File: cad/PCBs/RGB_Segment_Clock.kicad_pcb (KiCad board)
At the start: 2 copper layers, 7 parts, among them J1 TYPE-C-31-M-12, U1 BH1750FVI-TR, U2 HDC2080

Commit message: Initial Digit Schematic and Layout
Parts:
- added C1: 0.1 uF, Capacitor_SMD:C_0805_2012Metric, F.Cu at (176.9, 55.0)
- added C10: 0.1 uF, Capacitor_SMD:C_0805_2012Metric, F.Cu at (204.0, 25.4)
- added C11: 0.1 uF, Capacitor_SMD:C_0805_2012Metric, F.Cu at (218.9, 29.5)
- added C12: 0.1 uF, Capacitor_SMD:C_0805_2012Metric, F.Cu at (175.4, 133.0)
- added C13: 0.1 uF, Capacitor_SMD:C_0805_2012Metric, F.Cu at (198.5, 133.5)
- added C14: 0.1 uF, Capacitor_SMD:C_0805_2012Metric, F.Cu at (218.9, 132.5)
- added C2: 0.1 uF, Capacitor_SMD:C_0805_2012Metric, F.Cu at (197.0, 39.0)
- added C3: 0.1 uF, Capacitor_SMD:C_0805_2012Metric, F.Cu at (219.4, 55.0)
- added C4: 0.1 uF, Capacitor_SMD:C_0805_2012Metric, F.Cu at (220.4, 84.0)
- added C5: 0.1 uF, Capacitor_SMD:C_0805_2012Metric, F.Cu at (197.4, 103.0)
- added C6: 0.1 uF, Capacitor_SMD:C_0805_2012Metric, F.Cu at (177.9, 82.0)
- added C7: 0.1 uF, Capacitor_SMD:C_0805_2012Metric, F.Cu at (199.9, 69.5)
- added C8: 0.1 uF, Capacitor_SMD:C_0805_2012Metric, F.Cu at (177.1, 104.5)
- added C9: 0.1 uF, Capacitor_SMD:C_0805_2012Metric, F.Cu at (177.9, 29.5)
- added D2: SS310, Diode_SMD:D_SOD-323F, F.Cu at (166.1, 74.5)
- added D3: SS310, Diode_SMD:D_SOD-323F, F.Cu at (231.4, 70.5)
- added J2: Digit_OUT, Connector_PinHeader_2.54mm:PinHeader_1x06_P2.54mm_Horizontal, F.Cu at (239.1, 55.1)
- added LED1: DIGIT-A, LED_SMD:LED_SK6812_PLCC4_5.0x5.0mm_P3.2mm, B.Cu at (218.6, 47.1)
- added LED10: BL-2, LED_SMD:LED_SK6812_PLCC4_5.0x5.0mm_P3.2mm, F.Cu at (198.5, 22.1)
- added LED11: BL-3, LED_SMD:LED_SK6812_PLCC4_5.0x5.0mm_P3.2mm, F.Cu at (220.0, 22.1)
- added LED12: BL-4, LED_SMD:LED_SK6812_PLCC4_5.0x5.0mm_P3.2mm, F.Cu at (177.0, 124.6)
- added LED13: BL-5, LED_SMD:LED_SK6812_PLCC4_5.0x5.0mm_P3.2mm, F.Cu at (199.5, 124.9)
- added LED14: BL-6, LED_SMD:LED_SK6812_PLCC4_5.0x5.0mm_P3.2mm, F.Cu at (220.0, 124.9)
- added LED2: DIGIT-B, LED_SMD:LED_SK6812_PLCC4_5.0x5.0mm_P3.2mm, B.Cu at (198.6, 31.6)
- added LED3: DIGIT-C, LED_SMD:LED_SK6812_PLCC4_5.0x5.0mm_P3.2mm, B.Cu at (177.0, 46.9)
- added LED4: DIGIT-D, LED_SMD:LED_SK6812_PLCC4_5.0x5.0mm_P3.2mm, B.Cu at (175.5, 76.1)
- added LED5: DIGIT-E, LED_SMD:LED_SK6812_PLCC4_5.0x5.0mm_P3.2mm, B.Cu at (198.0, 95.4)
- added LED6: DIGIT-F, LED_SMD:LED_SK6812_PLCC4_5.0x5.0mm_P3.2mm, B.Cu at (217.6, 73.9)
- added LED7: DIGIT-G, LED_SMD:LED_SK6812_PLCC4_5.0x5.0mm_P3.2mm, B.Cu at (195.5, 61.4)
- added LED8: DIGIT-H, LED_SMD:LED_SK6812_PLCC4_5.0x5.0mm_P3.2mm, B.Cu at (218.0, 96.6)
- added LED9: BL-1, LED_SMD:LED_SK6812_PLCC4_5.0x5.0mm_P3.2mm, F.Cu at (179.0, 21.6)
- added SZ720788W1: ~, SZ720788W:SZ720788W, B.Cu at (115.5, 39.1)
- added U3: BH1750FVI-TR, BH1750FVI-TR:XDCR_BH1750FVI-TR, B.Cu at (108.0, 21.5)
- added U4: HDC2080, Package_SON:Texas_PWSON-N6, B.Cu at (123.2, 20.9)
- added USB1: TYPE-C-31-M-12, TYPE-C-31-M-12:HRO_TYPE-C-31-M-12, F.Cu at (115.0, 135.0)
- D1: moved to B.Cu
- J1: value TYPE-C-31-M-12 -> Digit_IN; footprint TYPE-C-31-M-12:HRO_TYPE-C-31-M-12 -> Connector_PinHeader_2.54mm:PinHeader_1x06_P2.54mm_Horizontal
- U1: value BH1750FVI-TR -> 74HC595; footprint BH1750FVI-TR:XDCR_BH1750FVI-TR -> Package_DIP:DIP-16_W7.62mm_Socket
- U2: value HDC2080 -> 74HC595; footprint Package_SON:Texas_PWSON-N6 -> Package_DIP:DIP-16_W7.62mm_Socket
- moved R2 121.2 mm to (125.5, 128.2), turned to -90 degrees
- moved R1 114.0 mm to (105.5, 128.3), turned to 90 degrees
- moved J1 111.8 mm to (161.0, 55.0)
- moved D1 102.0 mm to (101.5, 122.0), turned to 180 degrees
- moved U2 97.7 mm to (131.8, 93.9), turned to 180 degrees
- moved U1 88.1 mm to (131.6, 70.7), turned to 180 degrees
- moved A1 79.4 mm to (110.5, 91.0)
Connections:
- R1 pad 2: Net-(J1-CC1) -> Net-(USB1-CC1)
- R2 pad 1: Net-(J1-CC2) -> Net-(USB1-CC2)
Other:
- board outline added: 145.5 x 124 mm

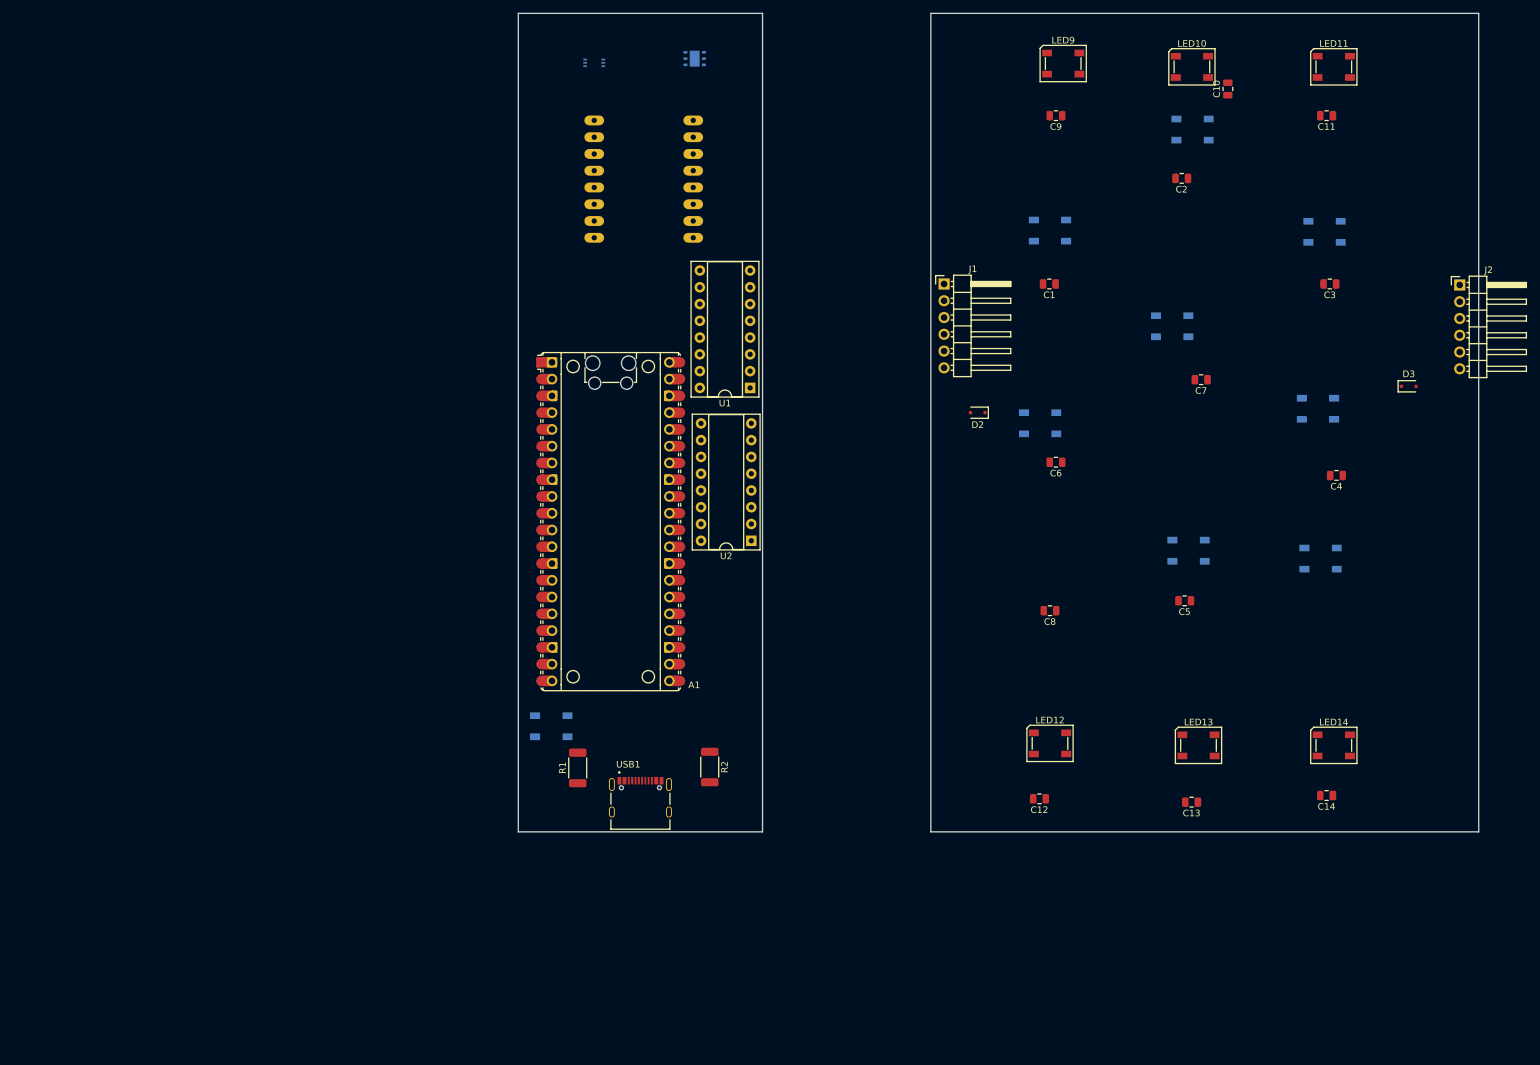
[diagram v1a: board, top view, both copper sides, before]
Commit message: Initial Digit Component Placement
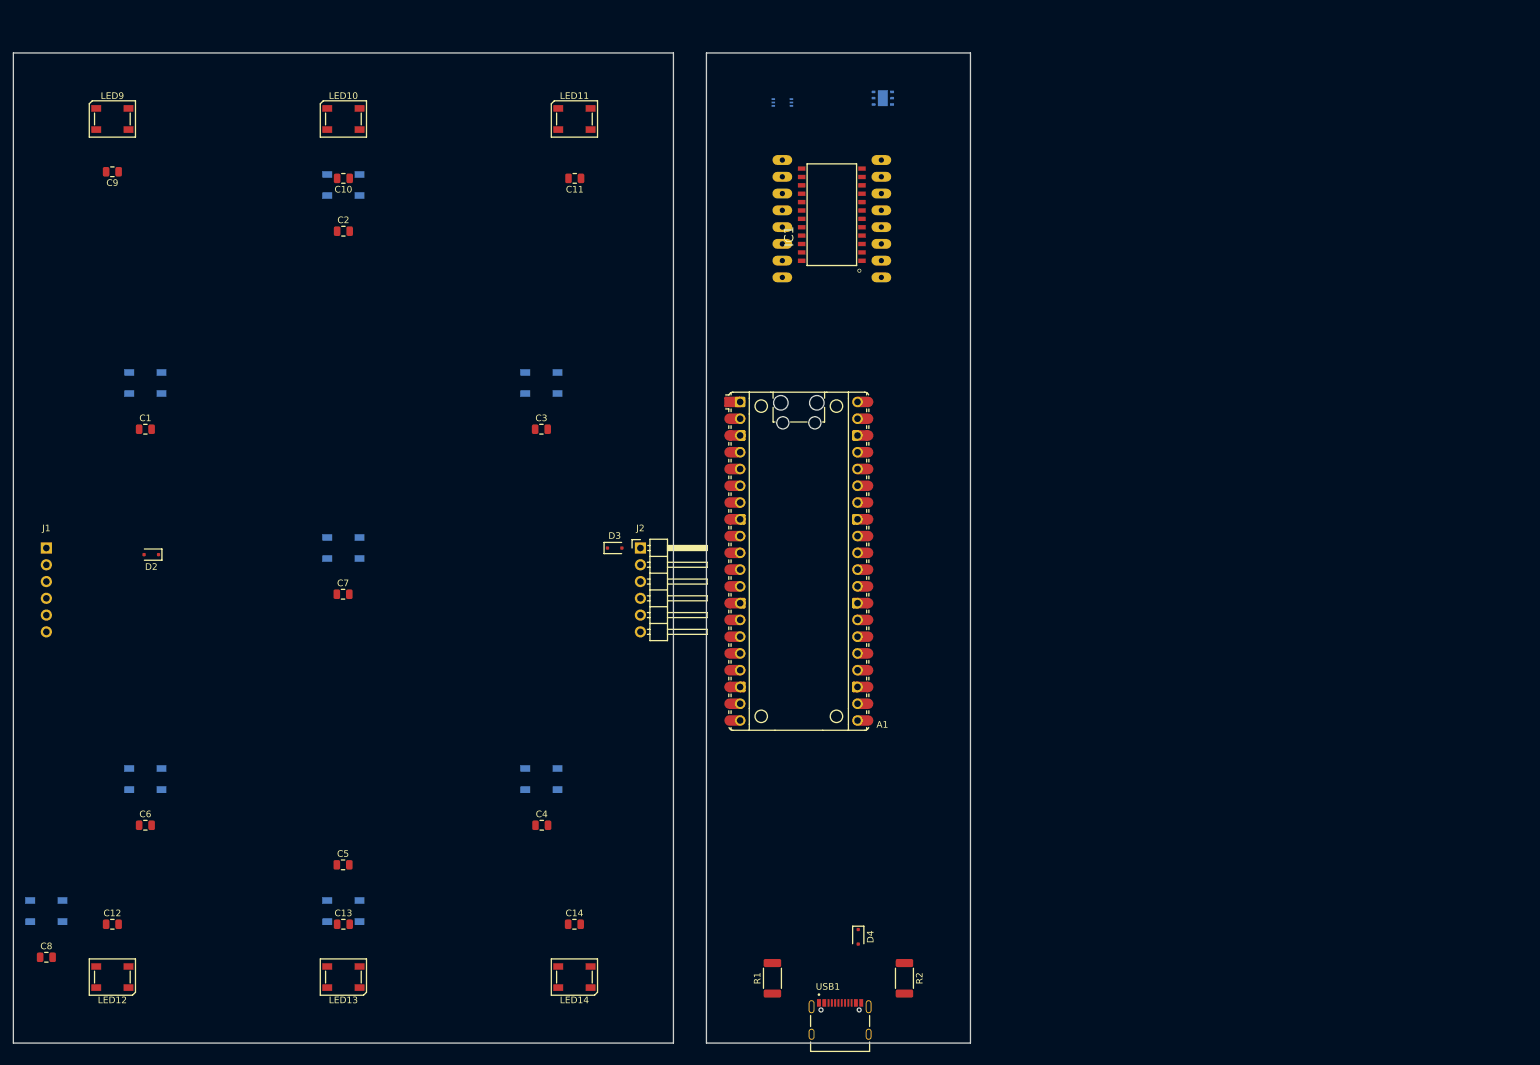
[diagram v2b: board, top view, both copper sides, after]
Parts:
- removed D1: SK6812, LED_SMD:LED_SK6812_PLCC4_5.0x5.0mm_P3.2mm
- removed U1, U2: 74HC595, Package_DIP:DIP-16_W7.62mm_Socket
- added D4: SS310, Diode_SMD:D_SOD-323F, F.Cu at (148.0, 153.9)
- added IC1: HT16K33, HT16K33:HT16K33, F.Cu at (144.0, 44.5)
- J1: moved to B.Cu
- moved LED8 200.3 mm to (25.0, 150.0)
- moved LED6 186.3 mm to (40.0, 130.0)
- moved LED1 180.1 mm to (40.0, 70.0)
- moved C8 160.9 mm to (25.0, 157.0), turned to 0 degrees
- moved C6 148.5 mm to (40.0, 137.0), turned to 0 degrees
- moved LED12 146.4 mm to (35.0, 160.0), turned to 180 degrees
- moved LED9 144.3 mm to (35.0, 30.0)
- moved C9 143.2 mm to (35.0, 38.0)
- moved J1 141.8 mm to (25.0, 95.0), turned to 180 degrees
- moved C12 141.7 mm to (35.0, 152.0), turned to 0 degrees
- moved LED5 139.2 mm to (70.0, 150.0)
- moved C1 138.7 mm to (40.0, 77.0), turned to 0 degrees
- moved C10 134.7 mm to (70.0, 39.0), turned to 180 degrees
- moved LED13 134.2 mm to (70.0, 160.0), turned to 180 degrees
- moved C7 134.0 mm to (70.0, 102.0), turned to 0 degrees
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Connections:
- A1 pad 39: unconnected-(A1-VSYS-Pad39) -> +5V
- USB1 pad A4_B9: +5V -> Net-(D4-A)
- USB1 pad B4_A9: +5V -> Net-(D4-A)
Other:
- board size 145.5 x 124 mm -> 145 x 150 mm

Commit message: Connected Controller Components, updated matrix footprint
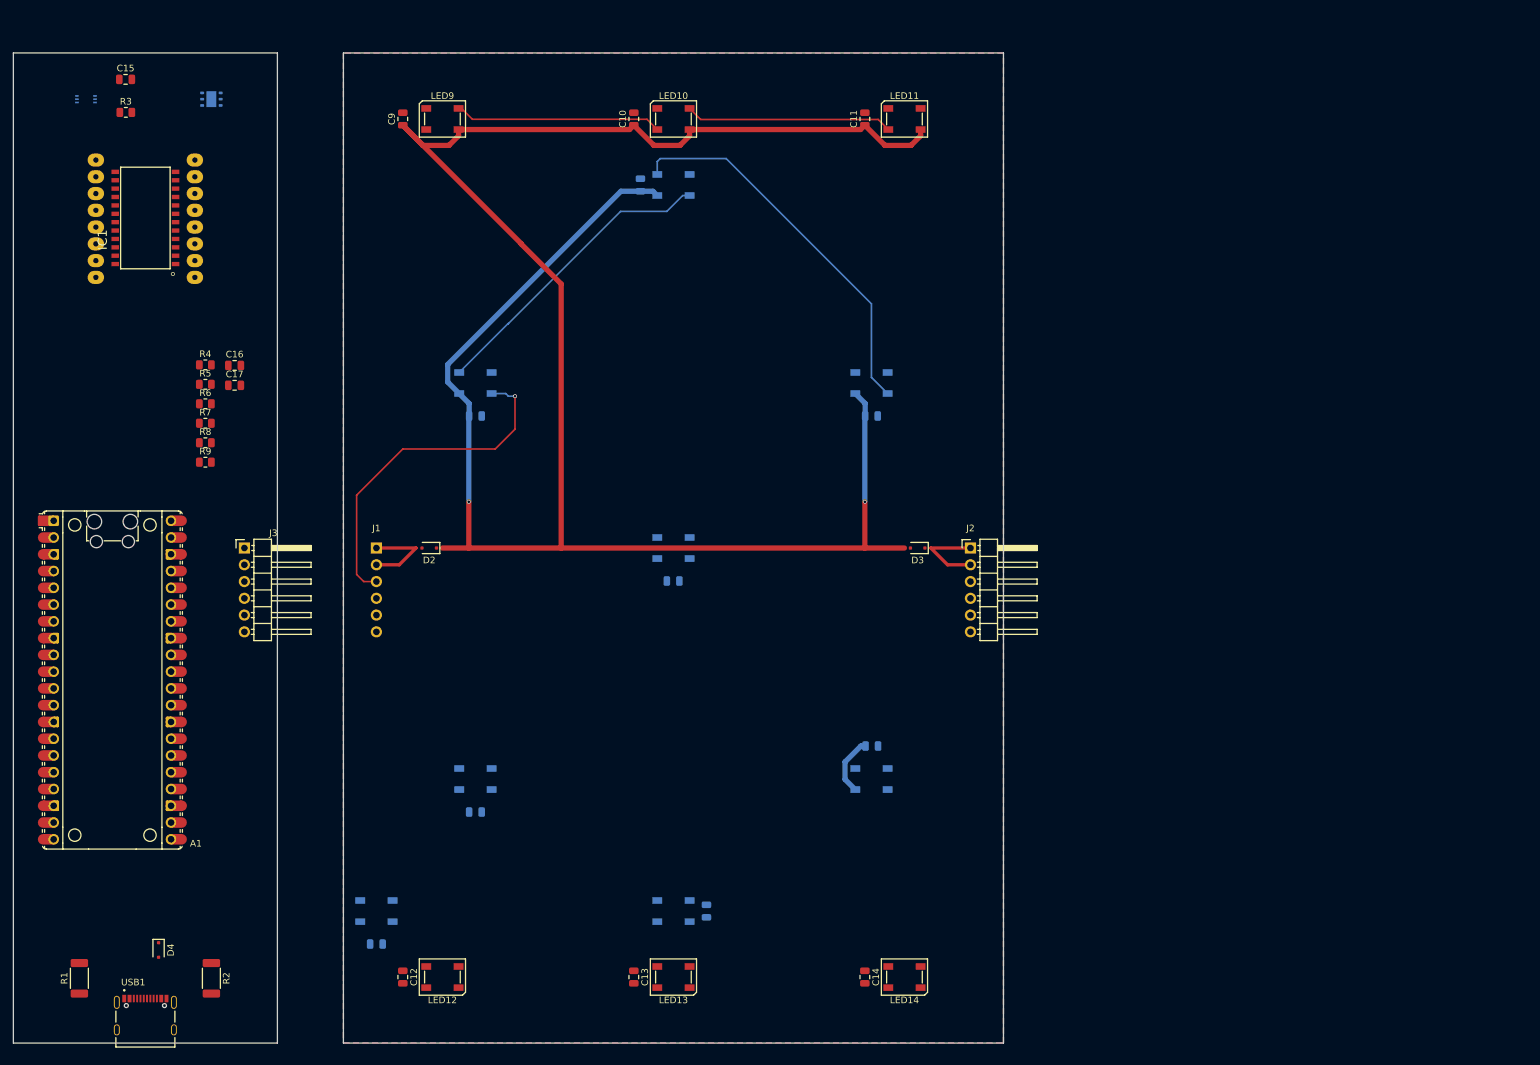
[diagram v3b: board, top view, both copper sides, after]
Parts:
- added C15: 0.1 uF, Capacitor_SMD:C_0805_2012Metric, F.Cu at (37.0, 24.0)
- added C16: 0.1 uF, Capacitor_SMD:C_0805_2012Metric, F.Cu at (53.5, 67.3)
- added C17: 10uF, Capacitor_SMD:C_0805_2012Metric, F.Cu at (53.5, 70.3)
- added J3: Controller_Out, Connector_PinHeader_2.54mm:PinHeader_1x06_P2.54mm_Horizontal, F.Cu at (55.0, 95.0)
- added R3: 4.7k, Resistor_SMD:R_0805_2012Metric, F.Cu at (37.0, 29.0)
- added R4: 4.7k, Resistor_SMD:R_0805_2012Metric, F.Cu at (49.1, 67.2)
- added R5: 4.7k, Resistor_SMD:R_0805_2012Metric, F.Cu at (49.1, 70.2)
- added R6: 4.7k, Resistor_SMD:R_0805_2012Metric, F.Cu at (49.1, 73.2)
- added R7: 4.7k, Resistor_SMD:R_0805_2012Metric, F.Cu at (49.1, 76.1)
- added R8: 4.7k, Resistor_SMD:R_0805_2012Metric, F.Cu at (49.1, 79.0)
- added R9: 4.7k, Resistor_SMD:R_0805_2012Metric, F.Cu at (49.1, 82.0)
- C1, C2, C3, C4, C5, C6, C7, C8: moved to B.Cu
- moved D4 106.0 mm to (42.0, 155.9)
- moved A1 105.5 mm to (35.0, 115.0)
- moved U3 105.5 mm to (31.0, 27.0)
- moved USB1 105.3 mm to (40.0, 168.0)
- moved R1 105.0 mm to (30.0, 160.2)
- moved R2 105.0 mm to (50.0, 160.2)
- moved IC1 104.0 mm to (40.0, 45.0)
- moved SZ720788W1 104.0 mm to (40.0, 45.0)
- moved U4 101.7 mm to (50.0, 27.0)
- moved C5 55.5 mm to (125.0, 150.0), turned to 90 degrees
- moved C4 51.4 mm to (150.1, 125.0)
- moved C1 50.0 mm to (90.0, 75.0)
- moved C3 50.0 mm to (150.0, 75.0)
- moved C6 50.0 mm to (90.0, 135.0)
- moved C7 50.0 mm to (120.0, 100.0)
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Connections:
- A1 pad 21: unconnected-(A1-GPIO16-Pad21) -> /Controller/DIGIT_OUT
- A1 pad 22: unconnected-(A1-GPIO17-Pad22) -> /Controller/BL_OUT
- A1 pad 24: unconnected-(A1-GPIO18-Pad24) -> /Controller/MATRIX_SDA
- A1 pad 25: unconnected-(A1-GPIO19-Pad25) -> /Controller/MATRIX_SCL
- A1 pad 26: unconnected-(A1-GPIO20-Pad26) -> /Controller/SENSOR_SDA
- A1 pad 27: unconnected-(A1-GPIO21-Pad27) -> /Controller/SENSOR_SCL
- A1 pad 33: unconnected-(A1-AGND-Pad33) -> GND
- A1 pad 36: unconnected-(A1-3V3-Pad36) -> +3.3V
- D2 pad 2: /Digit/VCC_IN -> +5V
- IC1 pad 1: unconnected-(IC1-VSS-Pad1) -> GND
- IC1 pad 14: unconnected-(IC1-ROW7/K6-Pad14) -> Net-(IC1-ROW7/K6)
- IC1 pad 15: unconnected-(IC1-ROW6/K5-Pad15) -> Net-(IC1-ROW6/K5)
- IC1 pad 16: unconnected-(IC1-ROW5/K4-Pad16) -> Net-(IC1-ROW5/K4)
- IC1 pad 17: unconnected-(IC1-ROW4/K3-Pad17) -> Net-(IC1-ROW4/K3)
- IC1 pad 18: unconnected-(IC1-ROW3/K2-Pad18) -> Net-(IC1-ROW3/K2)
- IC1 pad 19: unconnected-(IC1-ROW2/K1-Pad19) -> Net-(IC1-ROW2/K1)
- IC1 pad 2: unconnected-(IC1-COM0/AD-Pad2) -> Net-(IC1-COM0/AD)
- IC1 pad 20: unconnected-(IC1-ROW1/A0-Pad20) -> Net-(IC1-ROW1/A0)
- IC1 pad 21: unconnected-(IC1-ROW0/A1-Pad21) -> Net-(IC1-ROW0/A1)
- IC1 pad 22: unconnected-(IC1-SCL-Pad22) -> /Controller/MATRIX_SCL
- IC1 pad 23: unconnected-(IC1-SDA-Pad23) -> /Controller/MATRIX_SDA
- IC1 pad 24: unconnected-(IC1-VDD-Pad24) -> +3.3V
- IC1 pad 3: unconnected-(IC1-COM1/KS0-Pad3) -> Net-(IC1-COM1/KS0)
- IC1 pad 4: unconnected-(IC1-COM2/KS1-Pad4) -> Net-(IC1-COM2/KS1)
- IC1 pad 5: unconnected-(IC1-COM3/KS2-Pad5) -> Net-(IC1-COM3/KS2)
- IC1 pad 6: unconnected-(IC1-COM4-Pad6) -> Net-(IC1-COM4)
- IC1 pad 7: unconnected-(IC1-COM5-Pad7) -> Net-(IC1-COM5)
- IC1 pad 8: unconnected-(IC1-COM6-Pad8) -> Net-(IC1-COM6)
- IC1 pad 9: unconnected-(IC1-COM7-Pad9) -> Net-(IC1-COM7)
- J1 pad 1: /Digit/VCC_IN -> +5V
- J1 pad 2: /Digit/VCC_IN -> +5V
- J1 pad 3: /Digit/DIGIT_IN -> /Controller/DIGIT_OUT
- J1 pad 4: /Digit/BL_IN -> /Controller/BL_OUT
- LED1 pad 2: /Digit/DIGIT_IN -> /Controller/DIGIT_OUT
- LED9 pad 2: /Digit/BL_IN -> /Controller/BL_OUT
- SZ720788W1 pad 1: unconnected-(SZ720788W1-A1-Pad1) -> Net-(IC1-COM4)
- SZ720788W1 pad 10: unconnected-(SZ720788W1-B2-Pad10) -> Net-(IC1-ROW2/K1)
- SZ720788W1 pad 11: unconnected-(SZ720788W1-B3-Pad11) -> Net-(IC1-ROW4/K3)
- SZ720788W1 pad 12: unconnected-(SZ720788W1-B4-Pad12) -> Net-(IC1-COM3/KS2)
- SZ720788W1 pad 13: unconnected-(SZ720788W1-B5-Pad13) -> Net-(IC1-ROW7/K6)
- SZ720788W1 pad 14: unconnected-(SZ720788W1-B6-Pad14) -> Net-(IC1-COM1/KS0)
- SZ720788W1 pad 15: unconnected-(SZ720788W1-B7-Pad15) -> Net-(IC1-ROW5/K4)
- SZ720788W1 pad 16: unconnected-(SZ720788W1-B8-Pad16) -> Net-(IC1-ROW6/K5)
- SZ720788W1 pad 2: unconnected-(SZ720788W1-A2-Pad2) -> Net-(IC1-COM6)
- SZ720788W1 pad 3: unconnected-(SZ720788W1-A3-Pad3) -> Net-(IC1-ROW0/A1)
- SZ720788W1 pad 4: unconnected-(SZ720788W1-A4-Pad4) -> Net-(IC1-ROW1/A0)
- SZ720788W1 pad 5: unconnected-(SZ720788W1-A5-Pad5) -> Net-(IC1-COM7)
- SZ720788W1 pad 6: unconnected-(SZ720788W1-A6-Pad6) -> Net-(IC1-ROW3/K2)
- SZ720788W1 pad 7: unconnected-(SZ720788W1-A7-Pad7) -> Net-(IC1-COM5)
- SZ720788W1 pad 8: unconnected-(SZ720788W1-A8-Pad8) -> Net-(IC1-COM2/KS1)
- SZ720788W1 pad 9: unconnected-(SZ720788W1-B1-Pad9) -> Net-(IC1-COM0/AD)
- U3 pad 1: unconnected-(U3-VCC-Pad1) -> +3.3V
- U3 pad 2: unconnected-(U3-ADDR-Pad2) -> GND
- U3 pad 3: unconnected-(U3-GND-Pad3) -> GND
- U3 pad 4: unconnected-(U3-SDA-Pad4) -> /Controller/SENSOR_SDA
- U3 pad 5: unconnected-(U3-DVI-Pad5) -> Net-(U3-DVI)
- U3 pad 6: unconnected-(U3-SCL-Pad6) -> /Controller/SENSOR_SCL
- U4 pad 1: unconnected-(U4-SDA-Pad1) -> /Controller/SENSOR_SDA
- U4 pad 2: unconnected-(U4-GND-Pad2) -> GND
- U4 pad 3: unconnected-(U4-ADDR-Pad3) -> GND
- U4 pad 5: unconnected-(U4-VDD-Pad5) -> +3.3V
- U4 pad 6: unconnected-(U4-SCL-Pad6) -> /Controller/SENSOR_SCL
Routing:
- net +5V: track 0.00 -> 349.6 mm, vias 0 -> 2
- net Net-(LED2-DOUT): track 0.00 -> 58.3 mm
- net /Controller/DIGIT_OUT: track 0.00 -> 52.3 mm, vias 0 -> 1
- net Net-(LED1-DOUT): track 0.00 -> 46.0 mm
- net Net-(LED10-DIN): track 0.00 -> 31.6 mm
- net Net-(LED10-DOUT): track 0.00 -> 31.4 mm
- net /Digit/VCC_OUT: track 0.00 -> 13.1 mm
- added copper zone on B.Cu, net GND
- added copper zone on F.Cu, net GND
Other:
- board size 145 x 150 mm -> 150 x 150 mm
- rule pad_to_mask_clearance: 0 -> 0.038

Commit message: WIP Routing Controller
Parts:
- R1, R2: footprint Resistor_SMD:R_2010_5025Metric -> Resistor_SMD:R_0805_2012Metric
- moved R9 57.6 mm to (25.5, 29.5), turned to 180 degrees
- moved R8 57.1 mm to (25.5, 27.0)
- moved C16 44.3 mm to (25.5, 33.0)
- moved R5 44.0 mm to (44.0, 26.5)
- moved R4 38.6 mm to (44.0, 29.0), turned to 180 degrees
- moved R3 12.4 mm to (25.5, 24.5)
- moved R1 6.00 mm to (31.5, 166.0), turned to 0 degrees
- moved R2 6.00 mm to (48.5, 166.0), turned to 0 degrees
- moved C15 4.27 mm to (35.5, 28.0), turned to 90 degrees
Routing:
- net +3.3V: track 0.00 -> 131.2 mm, vias 0 -> 2
- net /Controller/SENSOR_SCL: track 0.00 -> 22.9 mm, vias 0 -> 2
- net GND: track 0.00 -> 16.4 mm, vias 0 -> 1
- net /Controller/SENSOR_SDA: track 0.00 -> 16.3 mm, vias 0 -> 1
- net Net-(U3-DVI): track 0.00 -> 13.4 mm, vias 0 -> 2
- net Net-(USB1-CC1): track 0.00 -> 8.00 mm
- net Net-(USB1-CC2): track 0.00 -> 7.47 mm
